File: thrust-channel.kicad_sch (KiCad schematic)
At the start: 11 parts, among them Q6 2SD1834T100, U17 MAX4210FEUA+, U18 FEMTA, U38 LM358

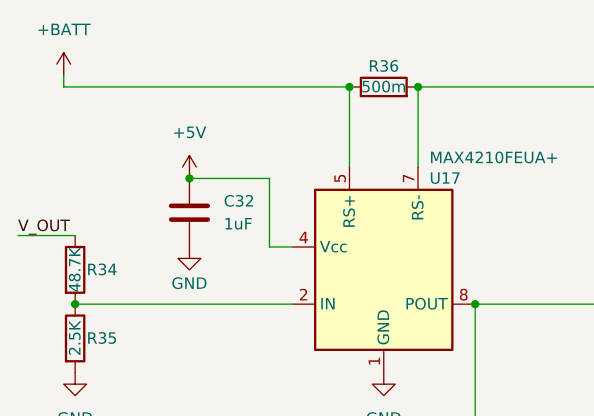
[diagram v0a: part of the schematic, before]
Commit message: page sizes
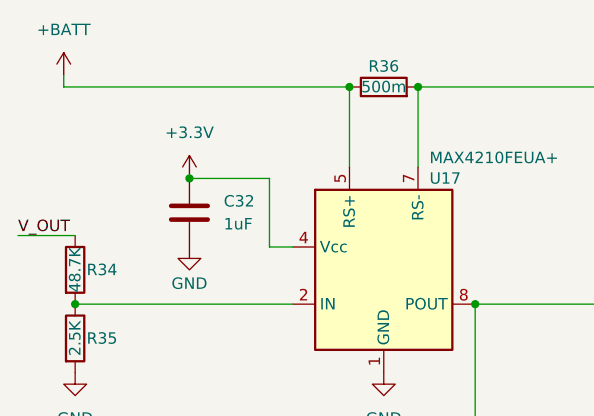
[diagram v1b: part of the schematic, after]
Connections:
- net +5V renamed +3.3V
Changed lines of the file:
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@@
 	(generator "eeschema")
 	(generator_version "8.0")
-	(paper "A4")
+	(paper "USLetter")
 	(junction
 		(at 57.15 63.5)
@@
 	)
 	(junction
-		(at 69.85 49.53)
-		(diameter 0)
-		(color 0 0 0 0)
-	)
-	(junction
 		(at 87.63 39.37)
 		(diameter 0)
@@
 	(junction
 		(at 116.84 87.63)
+		(diameter 0)
+		(color 0 0 0 0)
+	)
+	(junction
+		(at 69.85 49.53)
 		(diameter 0)
 		(color 0 0 0 0)
@@
 				(path "/838bf11c-36b7-41d7-9462-fe98a188d617/25504b25-63a2-43d8-9fee-c553eccedd0e/f663376f-9b89-41b3-aeca-9c6d61fe2c6e"
 					(reference "#PWR0138")
+					(unit 1)
+				)
+			)
+		)
+	)
+	(symbol
+		(lib_id "power:+3.3V")
+		(at 69.85 49.53 0)
+		(unit 1)
+		(exclude_from_sim no)
+		(in_bom yes)
+		(on_board yes)
+		(dnp no)
+		(fields_autoplaced yes)
+		(property "Reference" "#PWR070"
+			(at 69.85 53.34 0)
+			(effects
+				(font
+					(size 1.27 1.27)
+				)
+				(hide yes)
+			)
+		)
+		(property "Value" "+3.3V"
+			(at 69.85 44.45 0)
+			(effects
+				(font
+					(size 1.27 1.27)
+				)
+			)
+		)
+		(property "Footprint" ""
+			(at 69.85 49.53 0)
+			(effects
+				(font
+					(size 1.27 1.27)
+				)
+				(hide yes)
+			)
+		)
+		(property "Datasheet" ""
+			(at 69.85 49.53 0)
+			(effects
+				(font
+					(size 1.27 1.27)
+				)
+				(hide yes)
+			)
+		)
+		(property "Description" "Power symbol creates a global label with name \"+3.3V\""
+			(at 69.85 49.53 0)
+			(effects
+				(font
+					(size 1.27 1.27)
+				)
+				(hide yes)
+			)
+		)
+		(pin "1"
+		)
+		(instances
+			(project "femta-control"
+				(path "/838bf11c-36b7-41d7-9462-fe98a188d617/3bf849ef-bca6-4864-a347-fbff558d0891/49dafe5d-519c-49b1-88d9-ec8cb6df7648"
+					(reference "#PWR070")
+					(unit 1)
+				)
+				(path "/838bf11c-36b7-41d7-9462-fe98a188d617/3bf849ef-bca6-4864-a347-fbff558d0891/a6f30b1f-5689-4abf-92ce-ea5546b50948"
+					(reference "#PWR076")
+					(unit 1)
+				)
+				(path "/838bf11c-36b7-41d7-9462-fe98a188d617/3bf849ef-bca6-4864-a347-fbff558d0891/8de52c6a-44a2-4c3d-988b-6d07c6a566b2"
+					(reference "#PWR082")
+					(unit 1)
+				)
+				(path "/838bf11c-36b7-41d7-9462-fe98a188d617/3bf849ef-bca6-4864-a347-fbff558d0891/826227b2-3a4f-4a87-9419-7605bb4529f5"
+					(reference "#PWR088")
+					(unit 1)
+				)
+				(path "/838bf11c-36b7-41d7-9462-fe98a188d617/3bf849ef-bca6-4864-a347-fbff558d0891/47cd1a1a-1480-4eae-b9ce-a73cac0b3bdc"
+					(reference "#PWR094")
+					(unit 1)
+				)
+				(path "/838bf11c-36b7-41d7-9462-fe98a188d617/3bf849ef-bca6-4864-a347-fbff558d0891/37415780-54b9-4ed3-8ab8-f09b8d9e8267"
+					(reference "#PWR0100")
+					(unit 1)
+				)
+				(path "/838bf11c-36b7-41d7-9462-fe98a188d617/3bf849ef-bca6-4864-a347-fbff558d0891/ace2e429-6c02-47f3-a5a8-ce53fd79b4bb"
+					(reference "#PWR0106")
+					(unit 1)
+				)
+				(path "/838bf11c-36b7-41d7-9462-fe98a188d617/3bf849ef-bca6-4864-a347-fbff558d0891/b15c763d-24bc-4af2-a62c-4319be075b04"
+					(reference "#PWR0112")
+					(unit 1)
+				)
+				(path "/838bf11c-36b7-41d7-9462-fe98a188d617/25504b25-63a2-43d8-9fee-c553eccedd0e/193305be-6cda-4233-81aa-0afa66e3e4ce"
+					(reference "#PWR0130")
+					(unit 1)
+				)
+				(path "/838bf11c-36b7-41d7-9462-fe98a188d617/25504b25-63a2-43d8-9fee-c553eccedd0e/f663376f-9b89-41b3-aeca-9c6d61fe2c6e"
+					(reference "#PWR0136")
+					(unit 1)
+				)
+				(path "/838bf11c-36b7-41d7-9462-fe98a188d617/c8752098-45e2-4d20-a718-e7a412b889c5/193305be-6cda-4233-81aa-0afa66e3e4ce"
+					(reference "#PWR0154")
+					(unit 1)
+				)
+				(path "/838bf11c-36b7-41d7-9462-fe98a188d617/c8752098-45e2-4d20-a718-e7a412b889c5/f663376f-9b89-41b3-aeca-9c6d61fe2c6e"
+					(reference "#PWR0160")
 					(unit 1)
 				)
@@
 					(unit 1)
 				)
-			)
-		)
-	)
-	(symbol
-		(lib_id "power:+5V")
-		(at 69.85 49.53 0)
-		(unit 1)
-		(exclude_from_sim no)
-		(in_bom yes)
-		(on_board yes)
-		(dnp no)
-		(fields_autoplaced yes)
-		(property "Reference" "#PWR070"
-			(at 69.85 53.34 0)
-			(effects
-				(font
-					(size 1.27 1.27)
-				)
-				(hide yes)
-			)
-		)
-		(property "Value" "+5V"
-			(at 69.85 44.45 0)
-			(effects
-				(font
-					(size 1.27 1.27)
-				)
-			)
-		)
-		(property "Footprint" ""
-			(at 69.85 49.53 0)
-			(effects
-				(font
-					(size 1.27 1.27)
-				)
-				(hide yes)
-			)
-		)
-		(property "Datasheet" ""
-			(at 69.85 49.53 0)
-			(effects
-				(font
-					(size 1.27 1.27)
-				)
-				(hide yes)
-			)
-		)
-		(property "Description" "Power symbol creates a global label with name \"+5V\""
-			(at 69.85 49.53 0)
-			(effects
-				(font
-					(size 1.27 1.27)
-				)
-				(hide yes)
-			)
-		)
-		(pin "1"
-		)
-		(instances
-			(project "femta-control"
-				(path "/838bf11c-36b7-41d7-9462-fe98a188d617/3bf849ef-bca6-4864-a347-fbff558d0891/49dafe5d-519c-49b1-88d9-ec8cb6df7648"
-					(reference "#PWR070")
-					(unit 1)
-				)
-				(path "/838bf11c-36b7-41d7-9462-fe98a188d617/3bf849ef-bca6-4864-a347-fbff558d0891/47cd1a1a-1480-4eae-b9ce-a73cac0b3bdc"
-					(reference "#PWR094")
-					(unit 1)
-				)
-				(path "/838bf11c-36b7-41d7-9462-fe98a188d617/3bf849ef-bca6-4864-a347-fbff558d0891/a6f30b1f-5689-4abf-92ce-ea5546b50948"
-					(reference "#PWR076")
-					(unit 1)
-				)
-				(path "/838bf11c-36b7-41d7-9462-fe98a188d617/3bf849ef-bca6-4864-a347-fbff558d0891/37415780-54b9-4ed3-8ab8-f09b8d9e8267"
-					(reference "#PWR0100")
-					(unit 1)
-				)
-				(path "/838bf11c-36b7-41d7-9462-fe98a188d617/3bf849ef-bca6-4864-a347-fbff558d0891/8de52c6a-44a2-4c3d-988b-6d07c6a566b2"
-					(reference "#PWR082")
-					(unit 1)
-				)
-				(path "/838bf11c-36b7-41d7-9462-fe98a188d617/3bf849ef-bca6-4864-a347-fbff558d0891/ace2e429-6c02-47f3-a5a8-ce53fd79b4bb"
-					(reference "#PWR0106")
-					(unit 1)
-				)
-				(path "/838bf11c-36b7-41d7-9462-fe98a188d617/3bf849ef-bca6-4864-a347-fbff558d0891/826227b2-3a4f-4a87-9419-7605bb4529f5"
-					(reference "#PWR088")
-					(unit 1)
-				)
-				(path "/838bf11c-36b7-41d7-9462-fe98a188d617/3bf849ef-bca6-4864-a347-fbff558d0891/b15c763d-24bc-4af2-a62c-4319be075b04"
-					(reference "#PWR0112")
-					(unit 1)
-				)
-				(path "/838bf11c-36b7-41d7-9462-fe98a188d617/c8752098-45e2-4d20-a718-e7a412b889c5/193305be-6cda-4233-81aa-0afa66e3e4ce"
-					(reference "#PWR0154")
-					(unit 1)
-				)
-				(path "/838bf11c-36b7-41d7-9462-fe98a188d617/25504b25-63a2-43d8-9fee-c553eccedd0e/193305be-6cda-4233-81aa-0afa66e3e4ce"
-					(reference "#PWR0130")
-					(unit 1)
-				)
-				(path "/838bf11c-36b7-41d7-9462-fe98a188d617/c8752098-45e2-4d20-a718-e7a412b889c5/f663376f-9b89-41b3-aeca-9c6d61fe2c6e"
-					(reference "#PWR0160")
-					(unit 1)
-				)
-				(path "/838bf11c-36b7-41d7-9462-fe98a188d617/25504b25-63a2-43d8-9fee-c553eccedd0e/f663376f-9b89-41b3-aeca-9c6d61fe2c6e"
-					(reference "#PWR0136")
-					(unit 1)
-				)

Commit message: schematic finished milestone
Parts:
- renumbered C32 to C34, R34 to R43, R35 to R44, R36 to R45, R37 to R46, R38 to R47, R39 to R48, U38 to U42

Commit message: capacitor footprints
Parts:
- C34: footprint (none) -> Capacitor_SMD:C_0603_1608Metric
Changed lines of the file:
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@@
 			)
 		)
-		(property "Footprint" ""
+		(property "Footprint" "Capacitor_SMD:C_0603_1608Metric"
 			(at 70.8152 57.15 0)
 			(effects

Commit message: add more footprints
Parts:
- R46, R47, R48: footprint (none) -> Resistor_SMD:R_0603_1608Metric
- U42: footprint (none) -> Package_SO:SOIC-8_3.9x4.9mm_P1.27mm
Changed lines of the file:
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@@
 			)
 		)
-		(property "Footprint" ""
+		(property "Footprint" "Resistor_SMD:R_0603_1608Metric"
 			(at 125.73 81.788 90)
 			(effects
@@
 			)
 		)
-		(property "Footprint" ""
+		(property "Footprint" "Package_SO:SOIC-8_3.9x4.9mm_P1.27mm"
 			(at 125.73 90.17 0)
 			(effects
@@
 			)
 		)
-		(property "Footprint" ""
+		(property "Footprint" "Resistor_SMD:R_0603_1608Metric"
 			(at 166.37 91.948 90)
 			(effects
@@
 			)
 		)
-		(property "Footprint" ""
+		(property "Footprint" "Resistor_SMD:R_0603_1608Metric"
 			(at 110.49 89.408 90)
 			(effects

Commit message: footprint selection
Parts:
- R43, R44: footprint (none) -> Resistor_SMD:R_0603_1608Metric
- R45: footprint (none) -> Resistor_SMD:R_0805_2012Metric
- U17: footprint (none) -> femta-control:uMAX-8
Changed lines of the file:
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@@
 			)
 		)
-		(property "Footprint" ""
+		(property "Footprint" "Resistor_SMD:R_0603_1608Metric"
 			(at 55.372 59.69 90)
 			(effects
@@
 			)
 		)
-		(property "Footprint" ""
+		(property "Footprint" "Resistor_SMD:R_0603_1608Metric"
 			(at 55.372 67.31 90)
 			(effects
@@
 			)
 		)
-		(property "Footprint" ""
+		(property "Footprint" "femta-control:uMAX-8"
 			(at 91.44 48.26 0)
 			(effects
@@
 			)
 		)
-		(property "Footprint" ""
+		(property "Footprint" "Resistor_SMD:R_0805_2012Metric"
 			(at 91.44 41.148 90)
 			(effects
